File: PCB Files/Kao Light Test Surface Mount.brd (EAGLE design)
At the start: 71.1 x 49.9 mm, 32 parts, among them T1 2N2222, Y1 16MHz

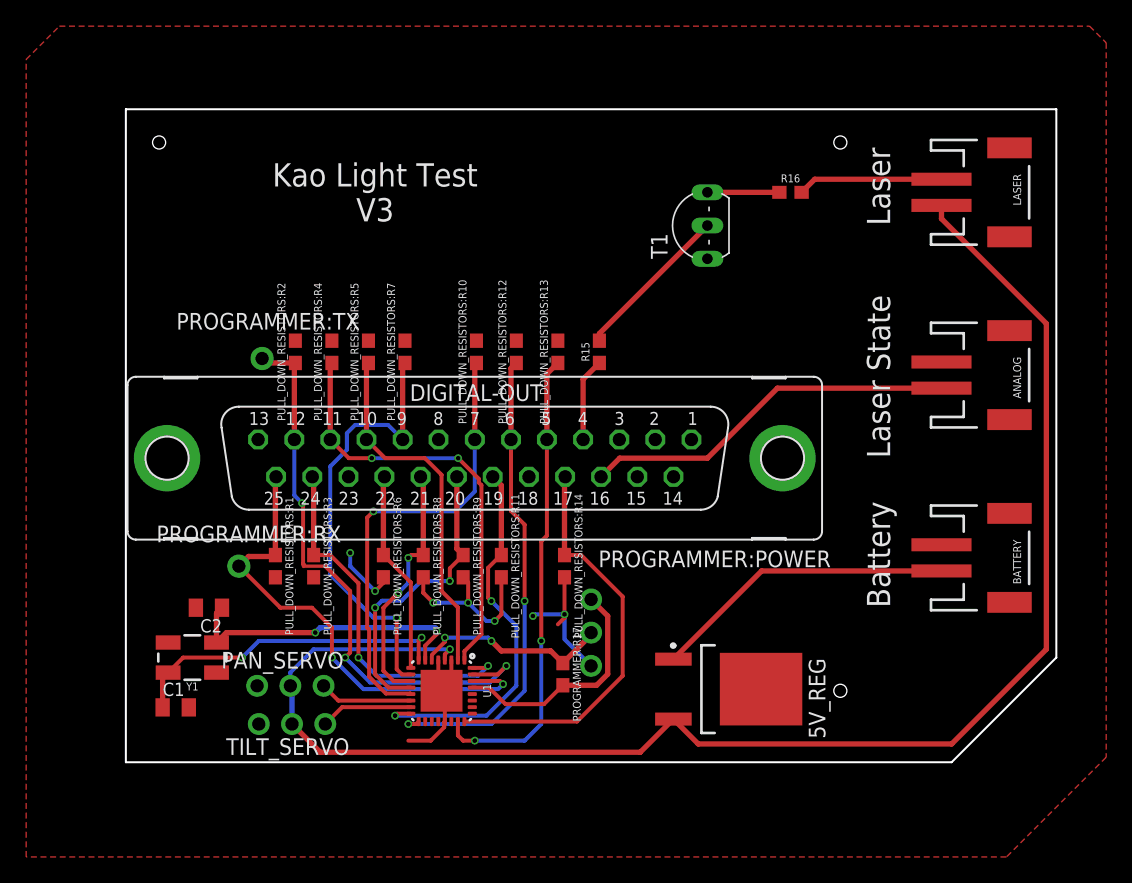
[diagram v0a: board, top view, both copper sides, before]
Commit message: feat: Adds status LEDs and Logo
Adds LEDs to indicate power from either the programming arduino's 5V
output or from the 5V regulator on the PCB. The LEDs should be different
colors and are labeled on the board. The logo is of the iSens logo
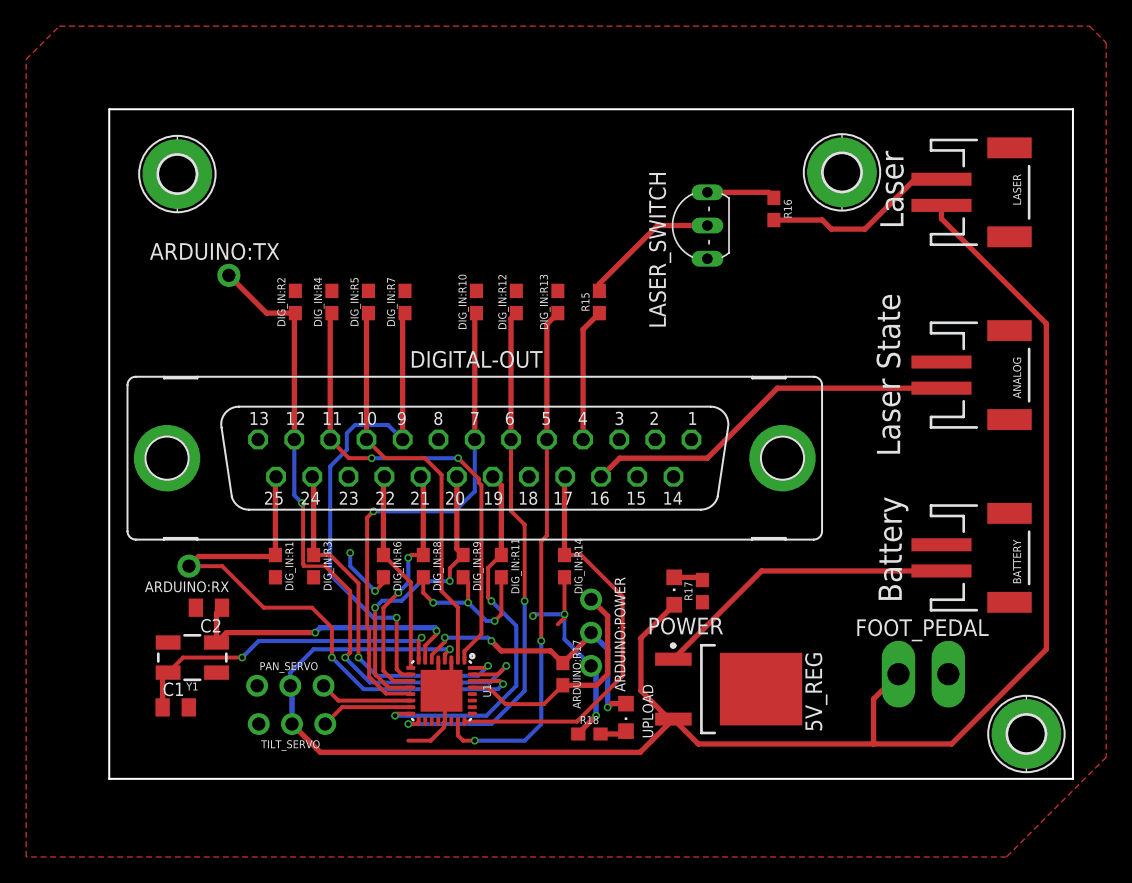
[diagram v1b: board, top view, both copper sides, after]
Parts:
- removed PROGRAMMER:RX, PROGRAMMER:TX: (no value), adafruit:1X01-CLEANBIG
- removed PULL_DOWN_RESISTORS:R10, PULL_DOWN_RESISTORS:R12, PULL_DOWN_RESISTORS:R13, PULL_DOWN_RESISTORS:R2, PULL_DOWN_RESISTORS:R4, PULL_DOWN_RESISTORS:R5, PULL_DOWN_RESISTORS:R7: 10k, SparkFun-Resistors:0603
- added ARDUINO:RX, ARDUINO:TX: (no value), adafruit:1X01-CLEANBIG
- added DIG_IN:R10, DIG_IN:R12, DIG_IN:R13, DIG_IN:R2, DIG_IN:R4, DIG_IN:R5, DIG_IN:R7: 10k, SparkFun-Resistors:0603
- added FOOT_PEDAL: TP2P2-38-17, testpad:P2-38-17
- added H1, H2, H3: MOUNT-PAD-ROUND2.8, holes:2,8-PAD
- added POWER, UPLOAD: (no value), adafruit:CHIPLED_0805
- added R17, R18: 220, SparkFun-Resistors:0603
- LASER_SWITCH: value 2N2222 -> 2N3904
- R16: value 200 -> 220
- moved R15 3.81 mm to (36.2, 34.8)
- moved R16 1.80 mm to (49.5, 41.9), turned to 270 degrees
- renumbered PROGRAMMER:POWER to ARDUINO:POWER, PROGRAMMER:R17 to ARDUINO:R17, PULL_DOWN_RESISTORS:R1 to DIG_IN:R1, PULL_DOWN_RESISTORS:R11 to DIG_IN:R11, PULL_DOWN_RESISTORS:R14 to DIG_IN:R14, PULL_DOWN_RESISTORS:R3 to DIG_IN:R3, PULL_DOWN_RESISTORS:R6 to DIG_IN:R6, PULL_DOWN_RESISTORS:R8 to DIG_IN:R8, PULL_DOWN_RESISTORS:R9 to DIG_IN:R9, T1 to LASER_SWITCH
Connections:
- new net N$5: POWER.C, R17.2
- new net N$7: R18.2, UPLOAD.C
- net 5VOUT: now also FOOT_PEDAL.TP-1, POWER.A
- net D1: now also ARDUINO:RX.1; no longer PROGRAMMER:RX.1
- net D10: now also DIG_IN:R10.1; no longer PULL_DOWN_RESISTORS:R10.1
- net D12: now also DIG_IN:R12.1; no longer PULL_DOWN_RESISTORS:R12.1
- net D13: now also DIG_IN:R13.1; no longer PULL_DOWN_RESISTORS:R13.1
- net D2: now also ARDUINO:TX.1, DIG_IN:R2.1; no longer PROGRAMMER:TX.1, PULL_DOWN_RESISTORS:R2.1
- net D4: now also DIG_IN:R4.1; no longer PULL_DOWN_RESISTORS:R4.1
- net D5: now also DIG_IN:R5.1; no longer PULL_DOWN_RESISTORS:R5.1
- net D7: now also DIG_IN:R7.1; no longer PULL_DOWN_RESISTORS:R7.1
- net GND: now also DIG_IN:R10.2, DIG_IN:R12.2, DIG_IN:R13.2, DIG_IN:R2.2, DIG_IN:R4.2, DIG_IN:R5.2, DIG_IN:R7.2, FOOT_PEDAL.TP-2, H1.B2,8, H2.B2,8, H3.B2,8, R17.1, R18.1; no longer PULL_DOWN_RESISTORS:R10.2, PULL_DOWN_RESISTORS:R12.2, PULL_DOWN_RESISTORS:R13.2, PULL_DOWN_RESISTORS:R2.2, PULL_DOWN_RESISTORS:R4.2, PULL_DOWN_RESISTORS:R5.2, PULL_DOWN_RESISTORS:R7.2
- net VIN: now also UPLOAD.A
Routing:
- net 5VOUT: track 118.5 -> 135.6 mm
- net VIN: track 15.2 -> 22.9 mm, vias 2 -> 3
- net D1: track 37.4 -> 45.0 mm
- net D2: track 44.6 -> 52.0 mm
- net GND: track 40.3 -> 46.2 mm, vias 7 -> 8
- net D12: track 36.5 -> 40.3 mm
- net D15: track 6.37 -> 10.2 mm
- net D5: track 27.5 -> 31.3 mm
- net D4: track 33.0 -> 36.8 mm
- net D13: track 36.2 -> 40.1 mm
- net D10: track 34.9 -> 38.7 mm
- net D7: track 33.9 -> 37.7 mm
- net N$6: track 11.1 -> 14.7 mm
- net N$5: track 0.00 -> 2.24 mm
- net N$7: track 0.00 -> 2.04 mm
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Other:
- board size 71.1 x 49.9 mm -> 73.7 x 51.2 mm
